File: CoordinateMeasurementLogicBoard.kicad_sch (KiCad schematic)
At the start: 17 parts, among them J1 DE9_Receptacle_MountingHoles, J2 DE9_Receptacle_MountingHoles, J3 DE9_Receptacle_MountingHoles, J4 DE9_Receptacle_MountingHoles, J5 DE9_Receptacle_MountingHoles, U1 AM2DS-0509SJZ

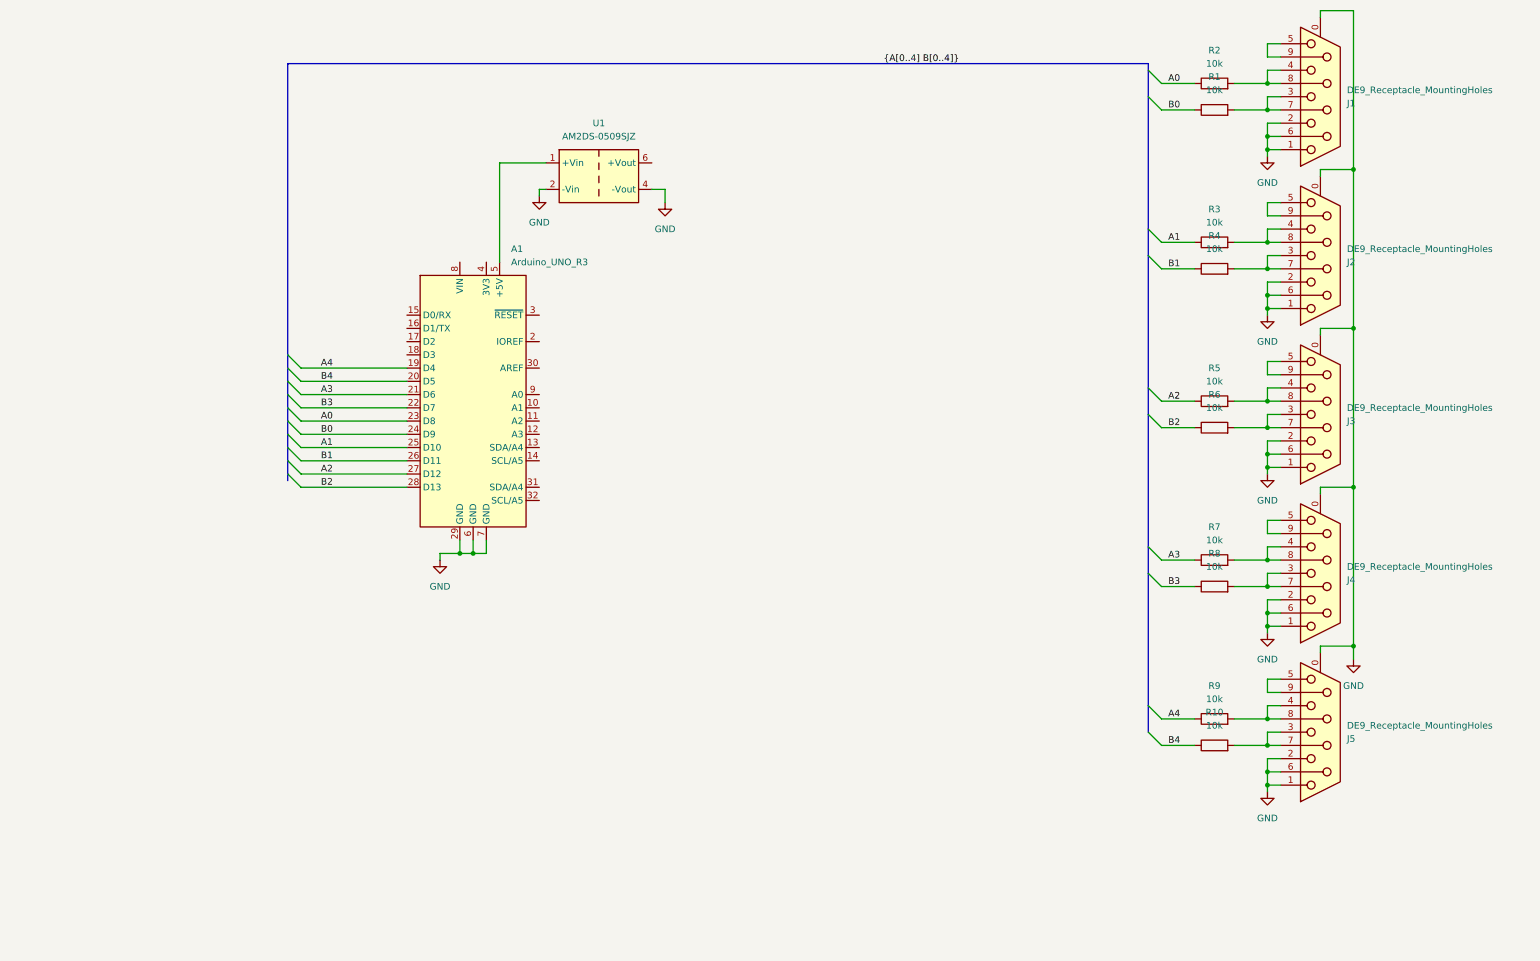
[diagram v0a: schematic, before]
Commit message: one protection circuit for all encoders; todo: select 2.2 ohm shunt, add caps for step up, LEDs
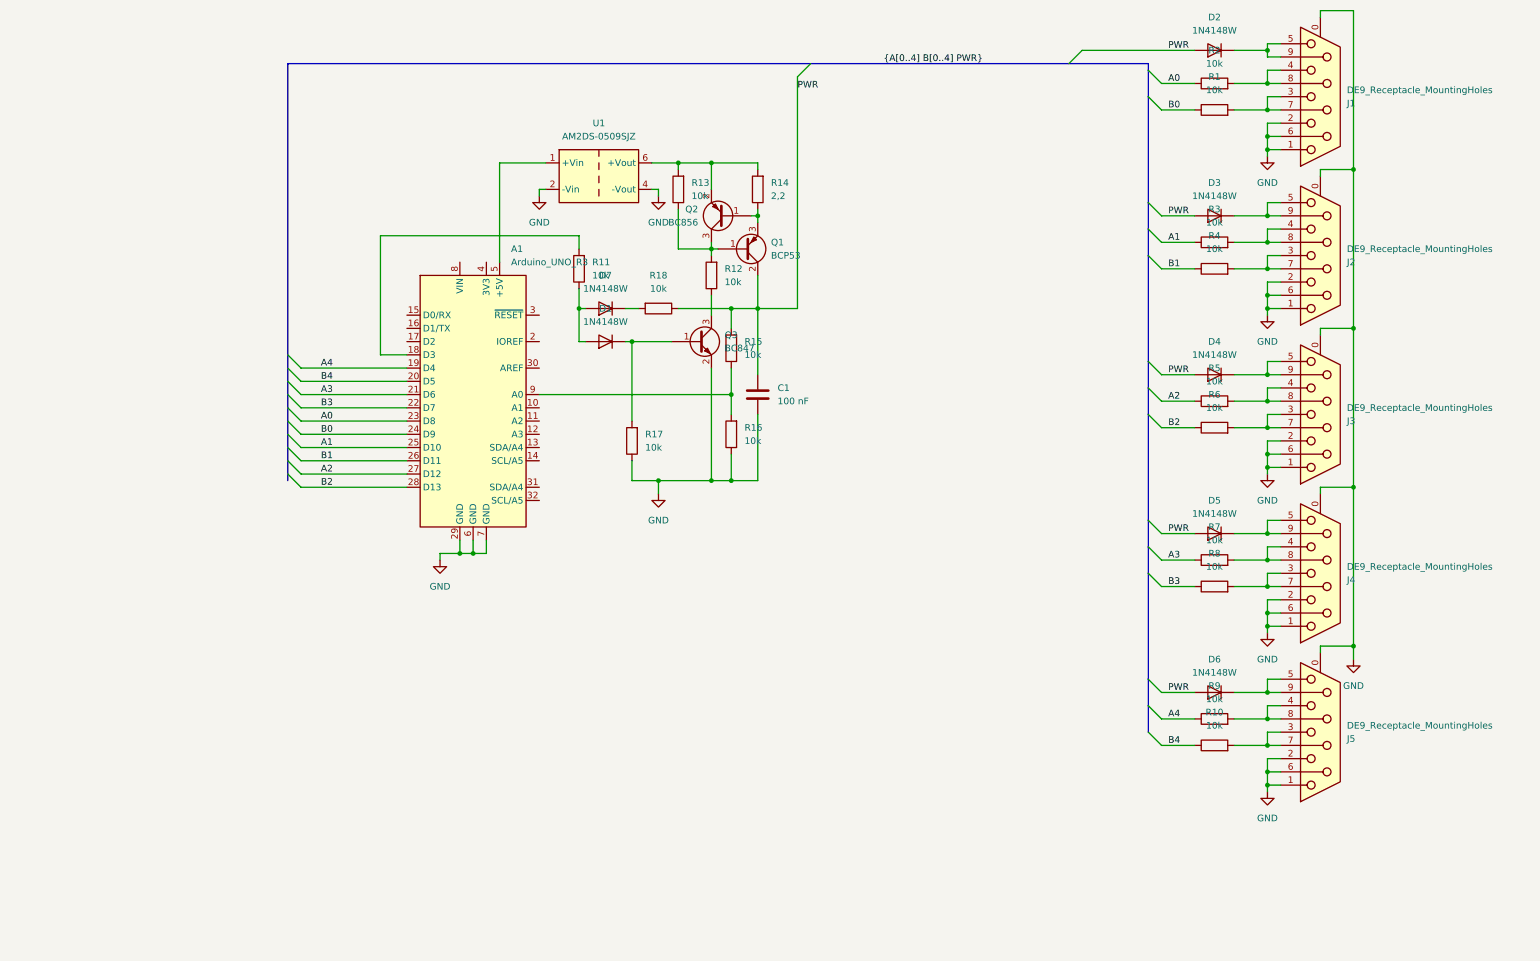
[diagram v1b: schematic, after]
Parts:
- added C1: 100 nF, symbol Device:C
- added D1, D2, D3, D4, D5, D6, D7: 1N4148W, Diode_SMD:D_SOD-123, symbol Diode:1N4148W
- added Q1: BCP53, Package_TO_SOT_SMD:SOT-223-3_TabPin2, symbol Transistor_BJT:BCP53
- added Q2: BC856, Package_TO_SOT_SMD:SOT-23, symbol Transistor_BJT:BC856
- added Q3: BC847, Package_TO_SOT_SMD:SOT-23, symbol Transistor_BJT:BC847
- added R11, R12, R13, R15, R16, R17, R18: 10k, Resistor_SMD:R_0805_2012Metric, symbol Device:R
- added R14: 2,2, Resistor_SMD:R_0805_2012Metric, symbol Device:R
- U1: Reichelt.de (none) -> AM2DS-0509SJZ
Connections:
- net GND: now also C1.2, Q3.2 (E), R16.1, R17.1
- net at J1.5, J1.9: now also D2.1 (K)
- net at J3.5, J3.9: now also D4.1 (K)
- net at A1.18 (D3): now also R11.2
- net at A1.9 (A0): now also R15.1, R16.2
- net at J4.5, J4.9: now also D5.1 (K)
- net at J2.5, J2.9: now also D3.1 (K)
- net at J5.5, J5.9: now also D6.1 (K)
- net at U1.6 (+Vout): now also Q2.2 (E), R13.2, R14.2
- new net: D7.1 (K), R18.2
- new net: D1.2 (A), D7.2 (A), R11.1
- new net: D1.1 (K), Q3.1 (B), R17.2
- new net: Q3.3 (C), R12.1
- new net: Q1.1 (B), Q2.3 (C), R12.2, R13.1
- new net: Q1.3 (E), Q2.1 (B), R14.1
- new net PWR: C1.1, D2.2 (A), D3.2 (A), D4.2 (A), D5.2 (A), D6.2 (A), Q1.2 (C), Q1.4 (C), R15.2, R18.1

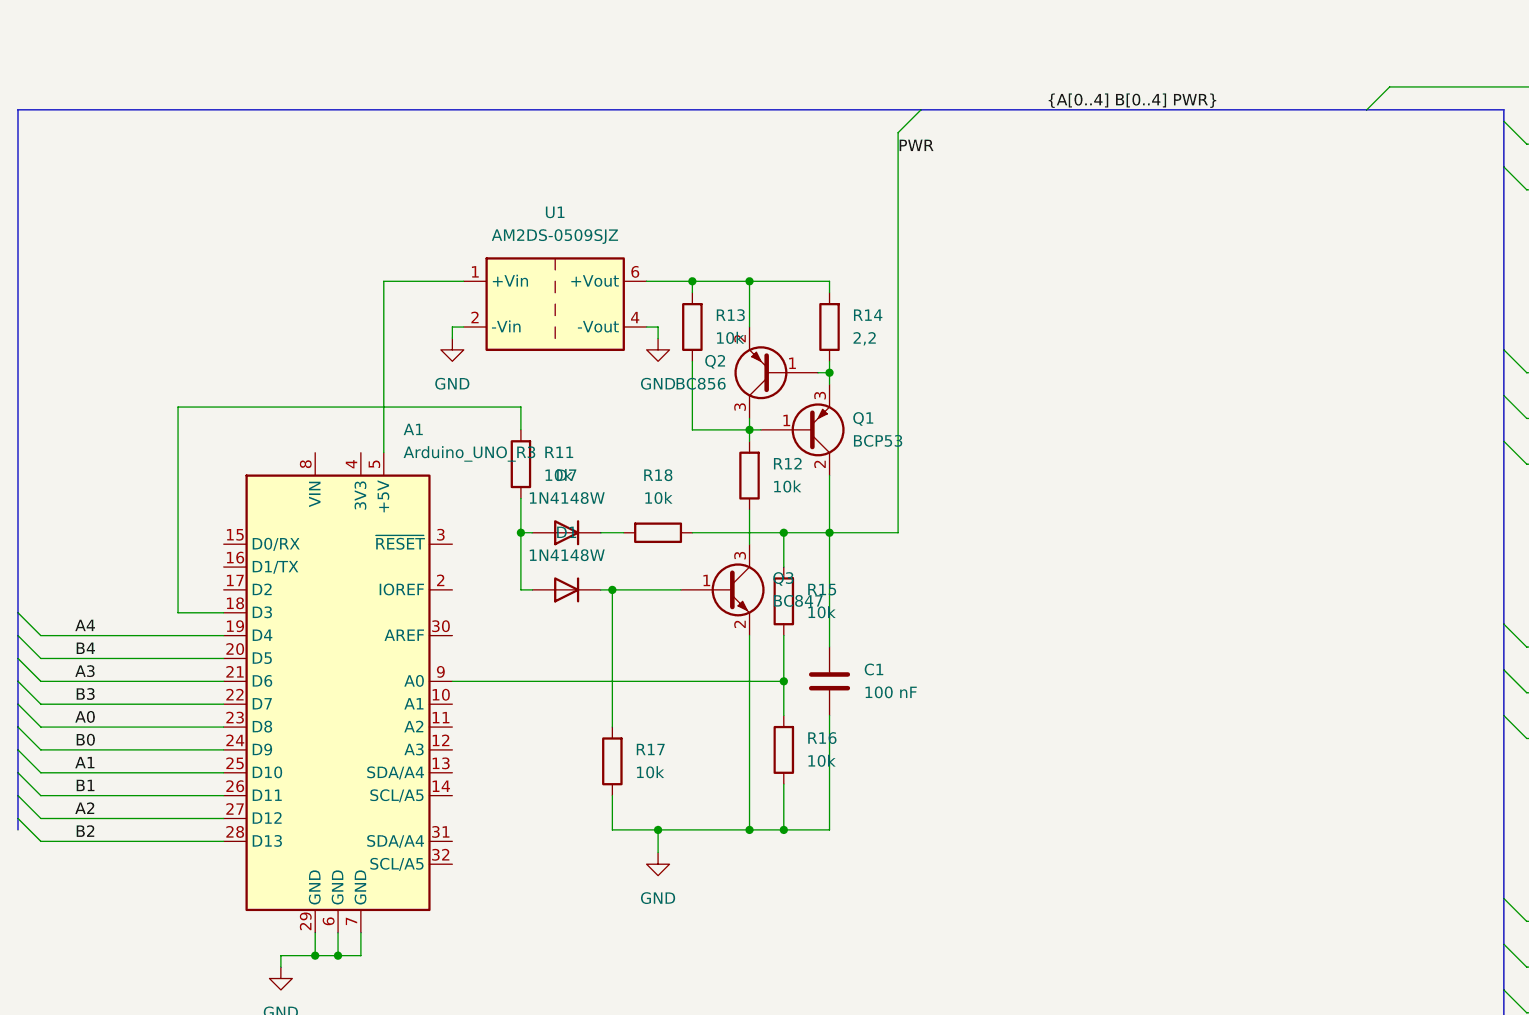
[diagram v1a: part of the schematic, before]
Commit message: one protection for all encoders; protection end transistor with 5 W, shunt 0.25 W; caps for dcdc converter
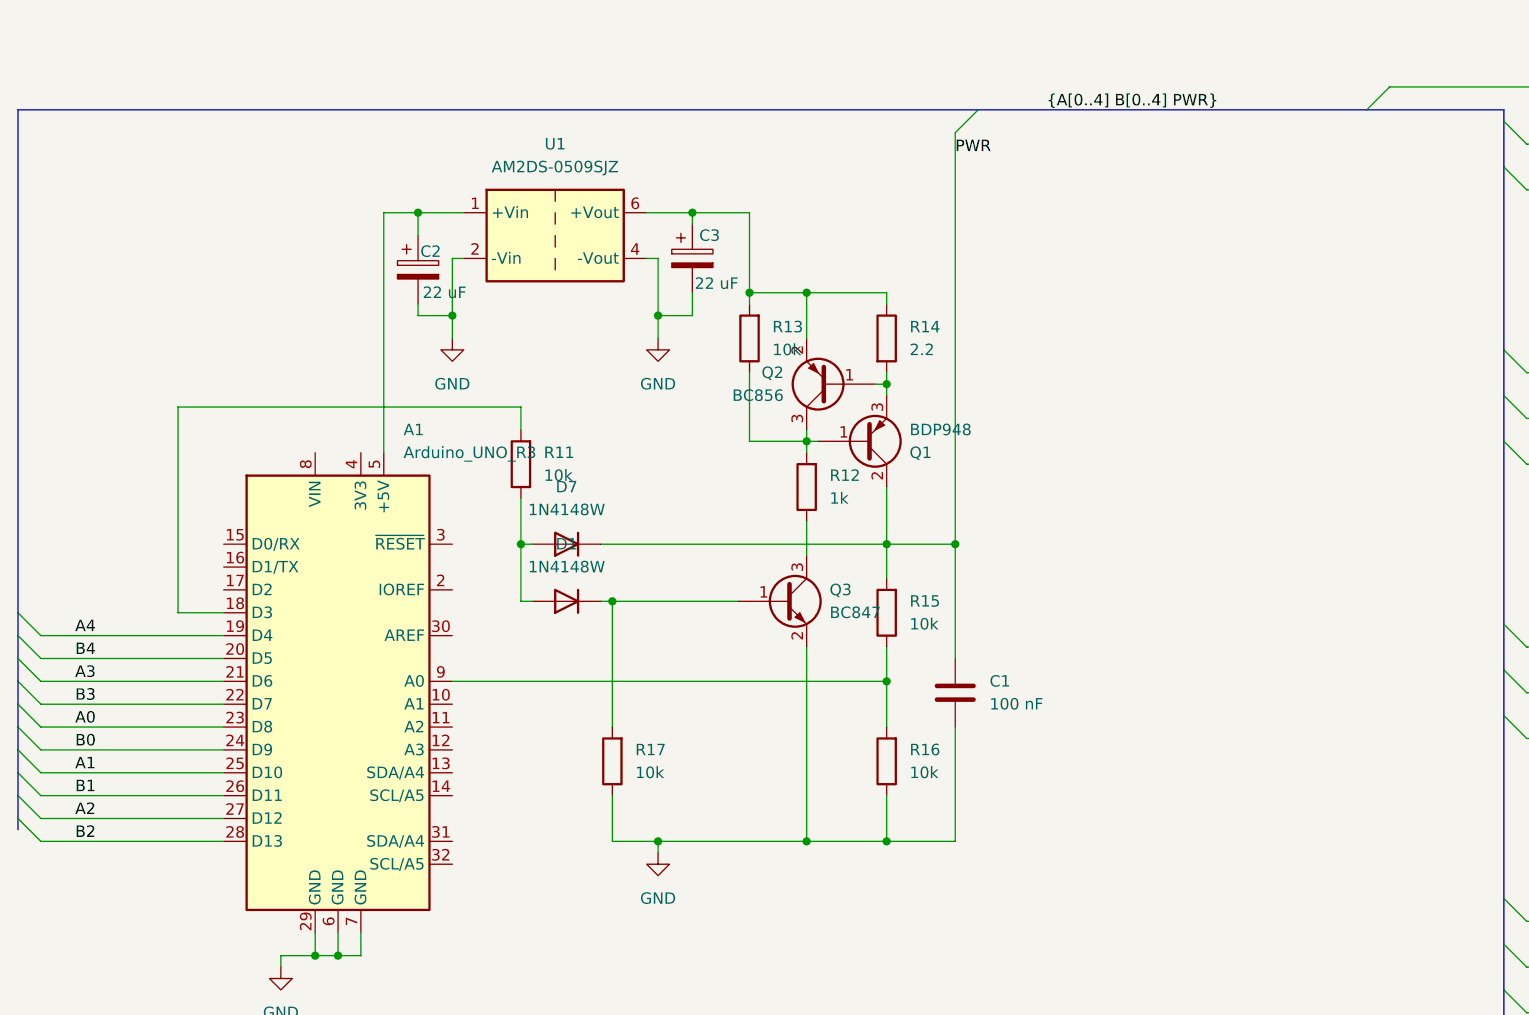
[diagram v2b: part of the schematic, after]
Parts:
- removed R18: 10k, Resistor_SMD:R_0805_2012Metric, symbol Device:R
- added C2, C3: 22 uF, Capacitor_THT:CP_Radial_D5.0mm_P2.00mm, symbol Device:C_Polarized
- Q1: value BCP53 -> BDP948; Reichelt.de BCP 53-16 SMD -> BDP 948 SMD
- R12: value 10k -> 1k; Reichelt.de SMD-0805 10,0K -> SMD-0805 1,0K
- R14: value 2,2 -> 2.2; footprint Resistor_SMD:R_0805_2012Metric -> Resistor_SMD:R_1206_3216Metric; Reichelt.de SMD-0805 2,2 -> SMD 1/4W 2,2
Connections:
- net GND: now also C2.2, C3.2
- net PWR: now also D7.1 (K)
- net at A1.5 (+5V), U1.1 (+Vin): now also C2.1
- net at Q1.3 (E), Q2.1 (B): now also R14.2; no longer R14.1
- net at Q2.2 (E), R13.2, U1.6 (+Vout): now also R14.1, C3.1; no longer R14.2
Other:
- moved on the sheet: C1, D1, D7, Q2, Q3, R12, R13, R15, R16, U1

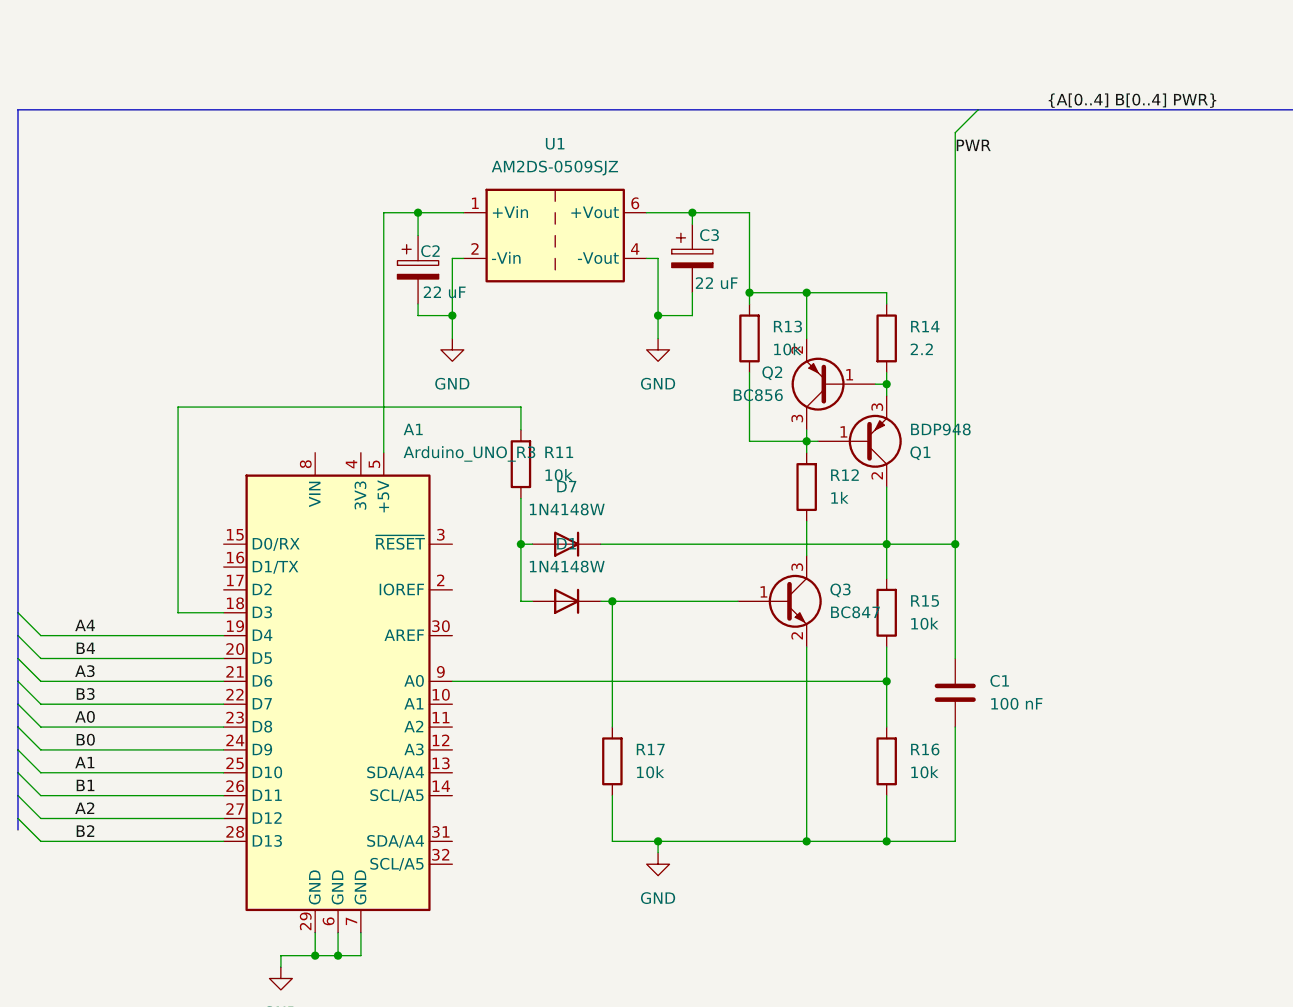
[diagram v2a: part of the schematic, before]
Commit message: fix: voltage divider; board nearly ready
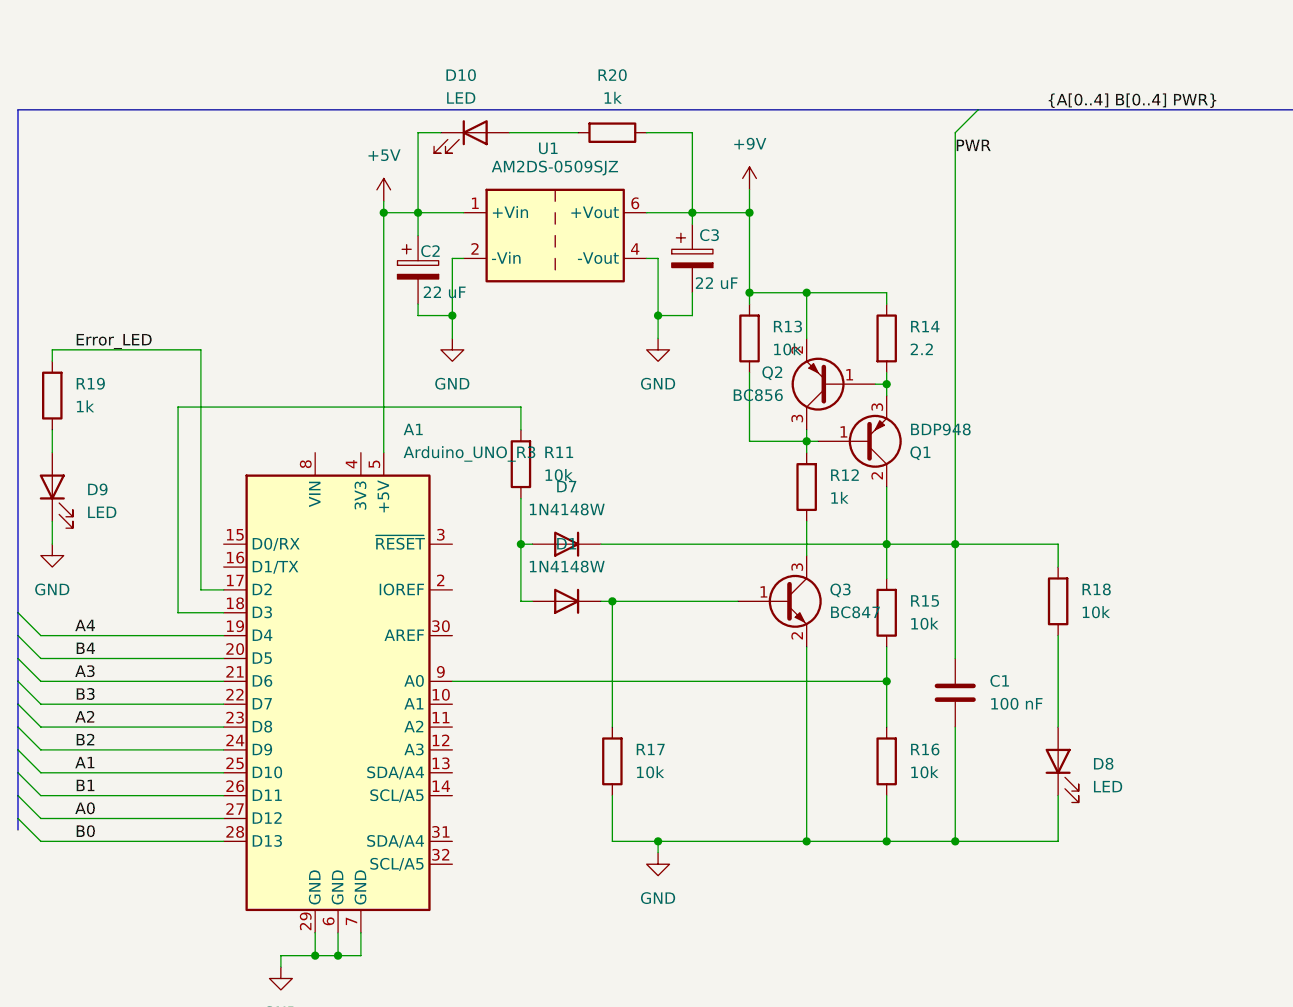
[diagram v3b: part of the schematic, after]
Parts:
- added D10, D8, D9: LED, LED_THT:LED_D5.0mm, symbol Device:LED
- added R18: 10k, Resistor_SMD:R_0805_2012Metric, symbol Device:R
- added R19, R20: 1k, Resistor_SMD:R_0805_2012Metric, symbol Device:R
- C1: footprint (none) -> Capacitor_SMD:C_0805_2012Metric
- J1, J2, J3, J4, J5: footprint (none) -> Connector_Dsub:DSUB-9_Female_Horizontal_P2.77x2.84mm_EdgePinOffset4.94mm_Housed_MountingHolesOffset7.48mm; Reichelt.de (none) -> D-SUB BU 09US
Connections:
- net A0: now also A1.27 (D12); no longer A1.23 (D8)
- net A2: now also A1.23 (D8); no longer A1.27 (D12)
- net B0: now also A1.28 (D13); no longer A1.24 (D9)
- net B2: now also A1.24 (D9); no longer A1.28 (D13)
- net GND: now also D8.1 (K), D9.1 (K)
- net PWR: now also R18.2
- net +5V: now reaches A1.5 (+5V), C2.1, U1.1 (+Vin)
- net +5V: now also D10.1 (K)
- net +9V: now reaches C3.1, Q2.2 (E), R13.2, R14.1, U1.6 (+Vout)
- net +9V: now also R20.1
- net Error_LED: now reaches A1.17 (D2)
- net Error_LED: now also R19.2
- new net: D10.2 (A), R20.2
- new net: D8.2 (A), R18.1
- new net: D9.2 (A), R19.1
